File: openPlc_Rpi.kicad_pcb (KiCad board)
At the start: 2 copper layers, 155 x 108 mm, 111 parts, among them J1 Raspberry_Pi_2_3, J10 Conn_01x04, J11 Conn_01x04, J12 Conn_01x04, J13 Conn_01x04, J14 Screw_Terminal_01x10, J2 Screw_Terminal_01x04, J3 Screw_Terminal_01x02, J5 Screw_Terminal_01x12, J7 Screw_Terminal_01x12, J8 Screw_Terminal_01x02, J9 Screw_Terminal_01x02, K1 G5LE-1, K2 G5LE-1, K3 G5LE-1, K4 G5LE-1, K5 G5LE-1, K6 G5LE-1, K7 G5LE-1, K8 G5LE-1, Q1 BSS123, Q2 2N7002, Q3 2N7002, U1 power_LM2576, U2 LTV-847, U3 LTV-847, U4 power_L7812_smd, U5 MAX481E, U6 ADS1018IDGS, U7 AMS1117-3.3, U8 ULN2803A

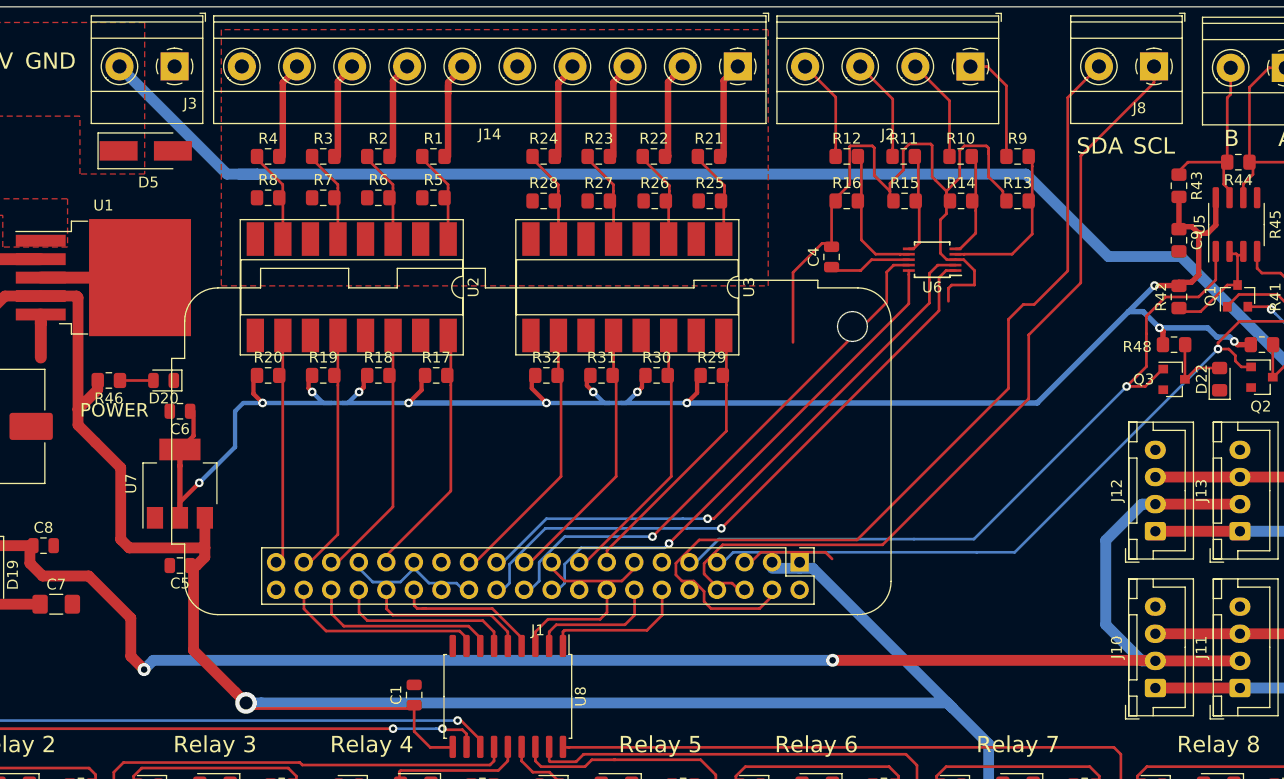
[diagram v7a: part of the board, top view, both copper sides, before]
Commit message: [easwaran] rough draft of routing for new orientation completed with no unconnected ratnests.
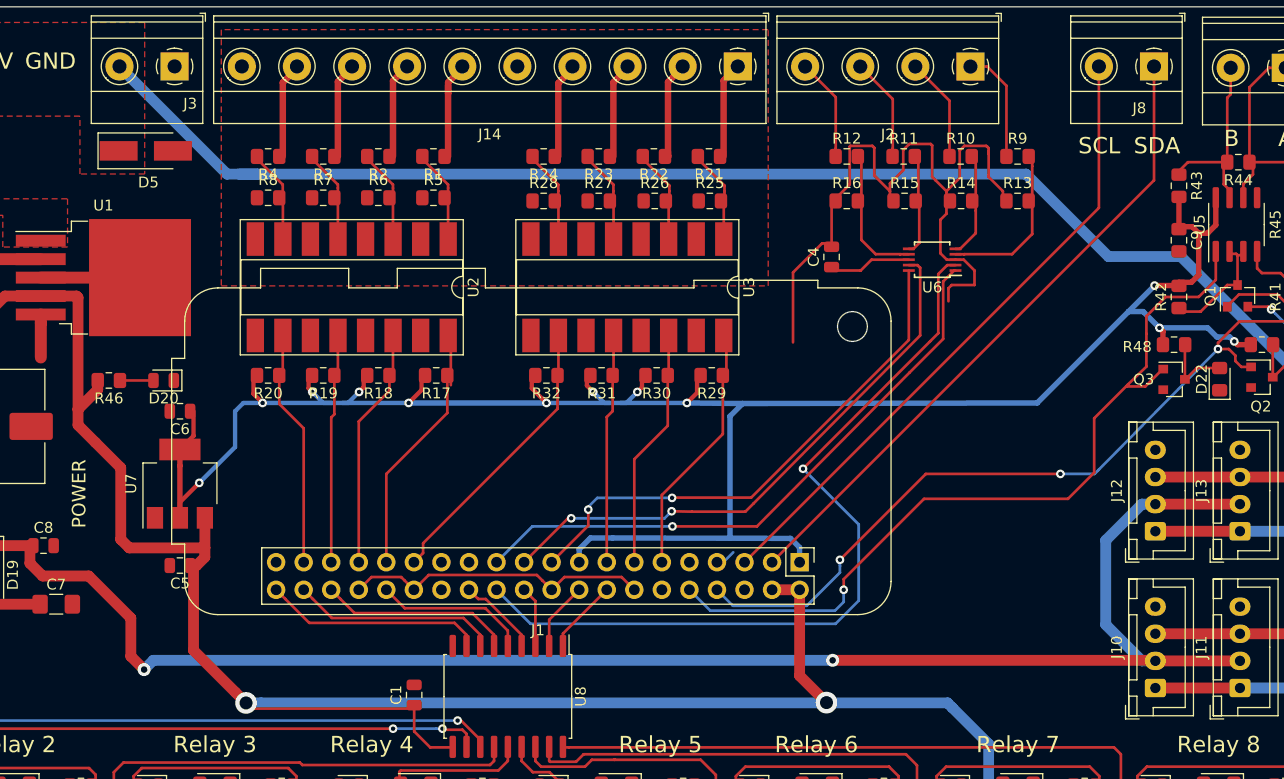
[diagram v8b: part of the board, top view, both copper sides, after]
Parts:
- J12: footprint Connector_JST:JST_XH_B4B-XH-A_1x04_P2.50mm_Vertical -> fossee_openplc:JST_XH_B4B-XH-A_1x04_P2.50mm_Vertical
- J14: footprint TerminalBlock_Phoenix:TerminalBlock_Phoenix_MKDS-1,5-10-5.08_1x10_P5.08mm_Horizontal -> fossee_openplc:TerminalBlock_Phoenix_MKDS-1,5-10-5.08_1x10_P5.08mm_Horizontal
- R1, R17, R18, R19, R2, R20, R21, R22, R23, R24, R25, R26, R27, R28, R29, R3, R30, R31, R32, R4, R5, R6, R7, R8: footprint Resistor_SMD:R_0805_2012Metric_Pad1.15x1.40mm_HandSolder -> fossee_openplc:R_0805_2012Metric_Pad1.15x1.40mm_HandSolder
- U2, U3: footprint Package_DIP:DIP-16_W8.89mm_SMDSocket_LongPads -> fossee_openplc:DIP-16_W8.89mm_SMDSocket_LongPads
- turned R1 to 180 degrees
- turned R17 to 180 degrees
- turned R18 to 180 degrees
- turned R19 to 180 degrees
- turned R2 to 180 degrees
- turned R20 to 180 degrees
- turned R21 to 180 degrees
- turned R22 to 180 degrees
- turned R23 to 180 degrees
- turned R24 to 180 degrees
- turned R29 to 180 degrees
- turned R3 to 180 degrees
- turned R30 to 180 degrees
- turned R31 to 180 degrees
- turned R32 to 180 degrees
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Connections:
- J8 pad 1: SCL -> SDA
- J8 pad 2: SDA -> SCL
- R1 pad 1: Net-(R1-Pad1) -> Net-(J14-Pad6)
- R1 pad 2: Net-(J14-Pad6) -> Net-(R1-Pad2)
- R17 pad 1: +3V3 -> DI_3
- R17 pad 2: DI_3 -> +3V3
- R18 pad 1: +3V3 -> DI_2
- R18 pad 2: DI_2 -> +3V3
- R19 pad 1: +3V3 -> DI_1
- R19 pad 2: DI_1 -> +3V3
- R2 pad 1: Net-(R2-Pad1) -> Net-(J14-Pad7)
- R2 pad 2: Net-(J14-Pad7) -> Net-(R2-Pad2)
- R20 pad 1: +3V3 -> DI_0
- R20 pad 2: DI_0 -> +3V3
- R21 pad 1: Net-(R21-Pad1) -> Net-(J14-Pad1)
- R21 pad 2: Net-(J14-Pad1) -> Net-(R21-Pad2)
- R22 pad 1: Net-(R22-Pad1) -> Net-(J14-Pad2)
- R22 pad 2: Net-(J14-Pad2) -> Net-(R22-Pad2)
- R23 pad 1: Net-(R23-Pad1) -> Net-(J14-Pad3)
- R23 pad 2: Net-(J14-Pad3) -> Net-(R23-Pad2)
- R24 pad 1: Net-(R24-Pad1) -> Net-(J14-Pad4)
- R24 pad 2: Net-(J14-Pad4) -> Net-(R24-Pad2)
- R25 pad 2: Net-(R21-Pad1) -> Net-(R21-Pad2)
- R26 pad 2: Net-(R22-Pad1) -> Net-(R22-Pad2)
- R27 pad 2: Net-(R23-Pad1) -> Net-(R23-Pad2)
- R28 pad 2: Net-(R24-Pad1) -> Net-(R24-Pad2)
- R29 pad 1: +3V3 -> DI_7
- R29 pad 2: DI_7 -> +3V3
- R3 pad 1: Net-(R3-Pad1) -> Net-(J14-Pad8)
- R3 pad 2: Net-(J14-Pad8) -> Net-(R3-Pad2)
- R30 pad 1: +3V3 -> DI_6
- R30 pad 2: DI_6 -> +3V3
- R31 pad 1: +3V3 -> DI_5
- R31 pad 2: DI_5 -> +3V3
- R32 pad 1: +3V3 -> DI_4
- R32 pad 2: DI_4 -> +3V3
- R4 pad 1: Net-(R4-Pad1) -> Net-(J14-Pad9)
- R4 pad 2: Net-(J14-Pad9) -> Net-(R4-Pad2)
- R5 pad 2: Net-(R1-Pad1) -> Net-(R1-Pad2)
- R6 pad 2: Net-(R2-Pad1) -> Net-(R2-Pad2)
- R7 pad 2: Net-(R3-Pad1) -> Net-(R3-Pad2)
- R8 pad 2: Net-(R4-Pad1) -> Net-(R4-Pad2)
- U2 pad 1: Net-(R1-Pad1) -> Net-(R1-Pad2)
- U2 pad 3: Net-(R2-Pad1) -> Net-(R2-Pad2)
- U2 pad 5: Net-(R3-Pad1) -> Net-(R3-Pad2)
- U2 pad 7: Net-(R4-Pad1) -> Net-(R4-Pad2)
- U3 pad 1: Net-(R21-Pad1) -> Net-(R21-Pad2)
- U3 pad 3: Net-(R22-Pad1) -> Net-(R22-Pad2)
- U3 pad 5: Net-(R23-Pad1) -> Net-(R23-Pad2)
- U3 pad 7: Net-(R24-Pad1) -> Net-(R24-Pad2)
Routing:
- net +3V3: track 170.3 -> 206.9 mm
- net SCL: track 86.1 -> 59.2 mm
- net SDA: track 83.4 -> 60.3 mm
- net CS0: track 55.5 -> 74.9 mm
- net Net-(R21-Pad2): track 0.00 -> 9.49 mm
- net Net-(R21-Pad1): track 9.49 -> 0.00 mm
- net Net-(R22-Pad2): track 0.00 -> 9.49 mm
- net Net-(R22-Pad1): track 9.49 -> 0.00 mm
- net Net-(R24-Pad2): track 0.00 -> 9.43 mm
- net Net-(R24-Pad1): track 9.43 -> 0.00 mm
- net Net-(R23-Pad2): track 0.00 -> 9.43 mm
- net Net-(R23-Pad1): track 9.43 -> 0.00 mm
- net Net-(R4-Pad2): track 0.00 -> 9.43 mm
- net Net-(R4-Pad1): track 9.43 -> 0.00 mm
- net Net-(R3-Pad2): track 0.00 -> 9.43 mm
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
